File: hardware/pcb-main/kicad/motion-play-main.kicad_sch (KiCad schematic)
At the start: 21 parts, among them J3 LED_Strip, J4 Conn_01x05, J5 Conn_01x05, J6 Conn_01x05, U2 T-Display-S3

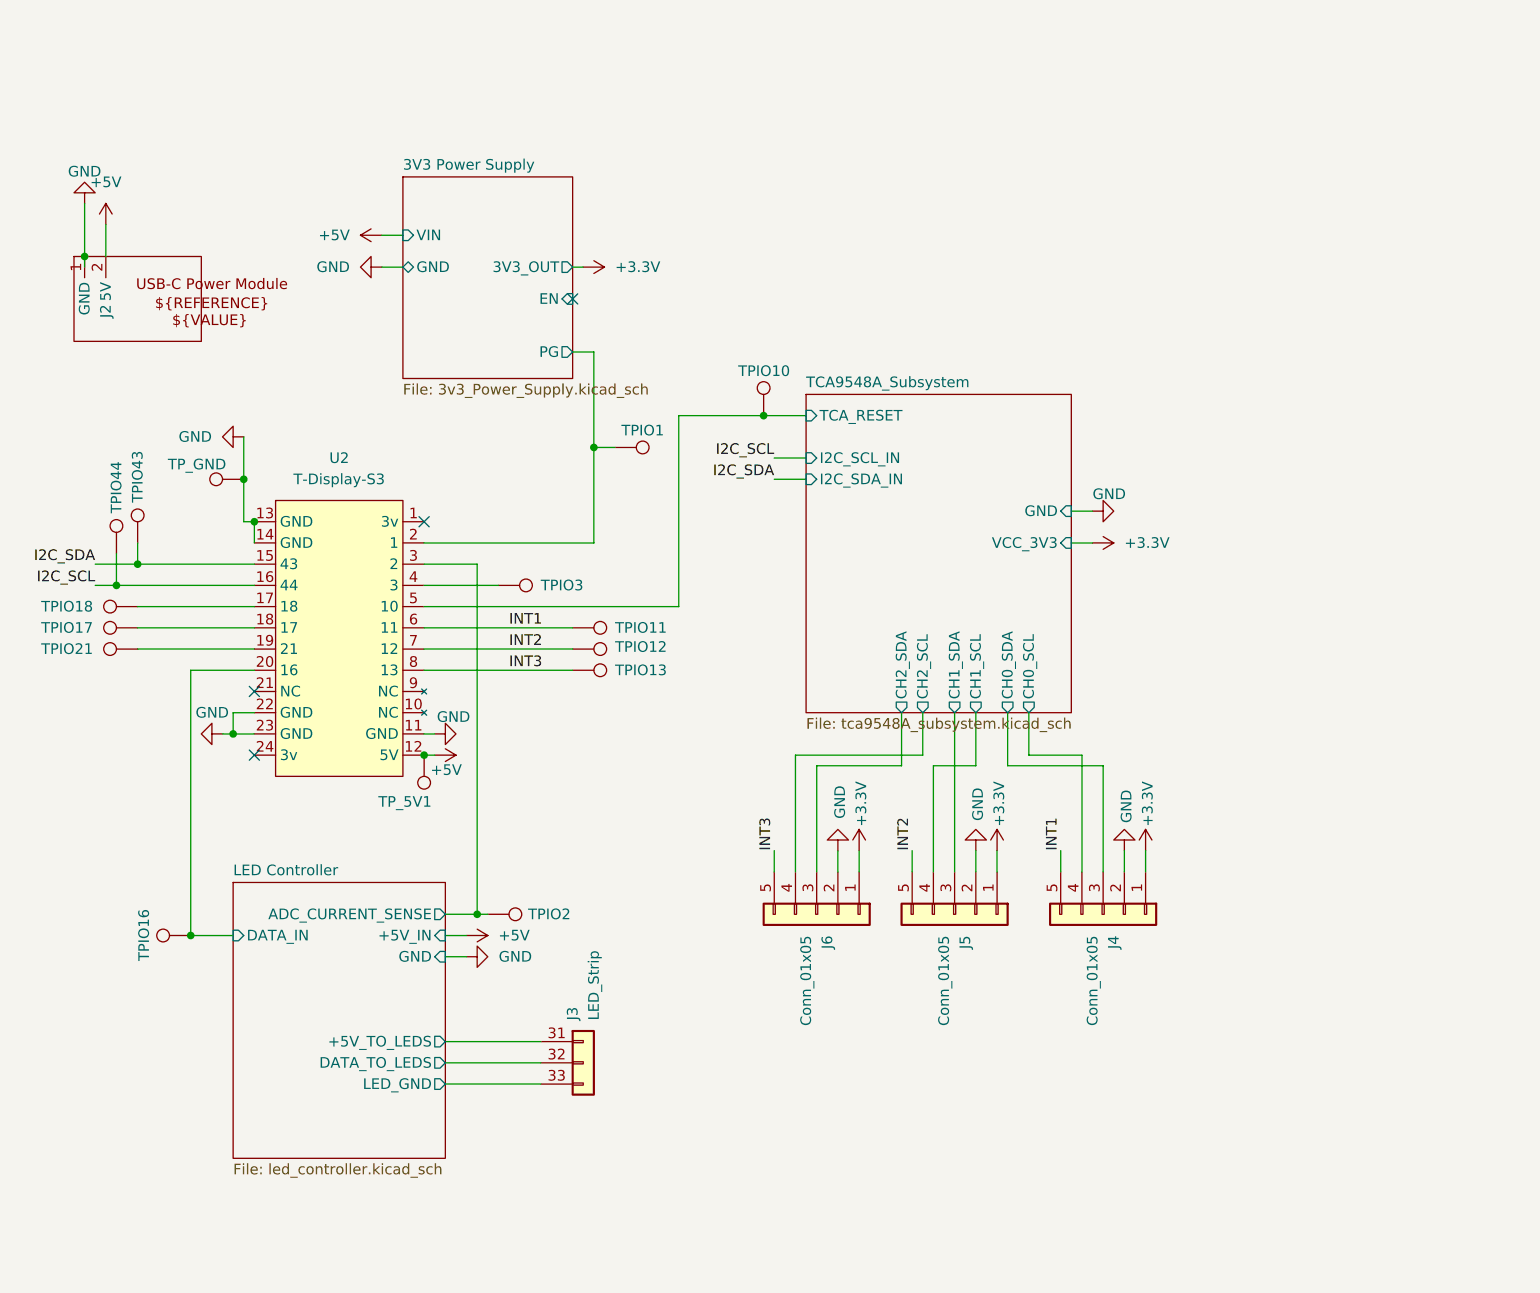
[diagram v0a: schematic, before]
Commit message: Updated to use ultra simplified 3v buck converter
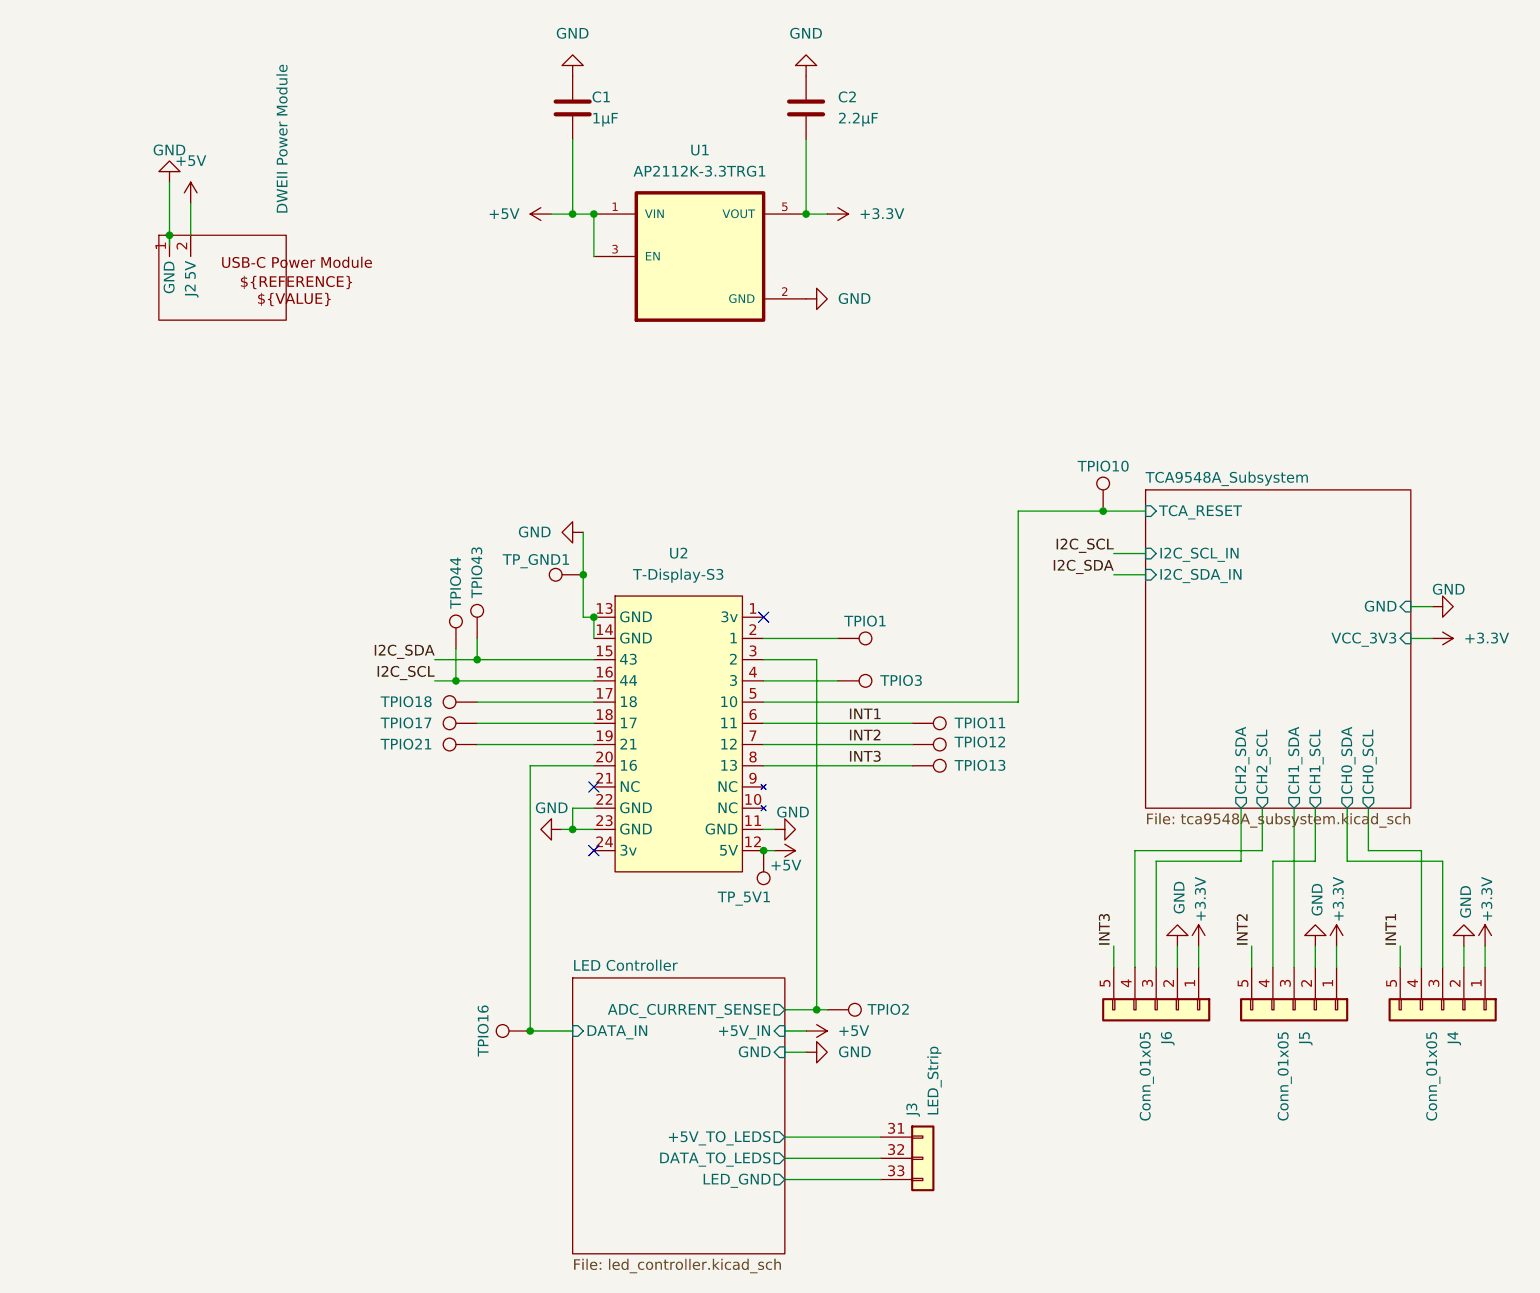
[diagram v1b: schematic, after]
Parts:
- added C1: 1µF, Capacitor_SMD:C_0603_1608Metric, symbol Device:C
- added C2: 2.2µF, Capacitor_SMD:C_0603_1608Metric, symbol Device:C
- added U1: AP2112K-3.3TRG1, AP2112K-3.3TRG1:SOT95P285X140-5N, symbol motion-play-symbols:AP2112K-3.3TRG1
- J2: value ~ -> DWEII Power Module
- renumbered TP_GND to TP_GND1
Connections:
- net +3.3V: now also C2.2, U1.5 (VOUT)
- net +5V: now also C1.2, U1.1 (VIN), U1.3 (EN)
- net GND: now also C1.1, C2.1, U1.2 (GND)
- net 3V3 Power Supply/PG: no longer names the net of TPIO1.1, U2.2 (1)
- no-connect marks 4 -> 3
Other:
- removed sheet 3V3 Power Supply
- title: (none) -> Motion Play Main Board
- moved on the sheet: J2, J3, J4, J5, J6, TPIO1, TPIO10, TPIO11, TPIO12, TPIO13, TPIO16, TPIO17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
